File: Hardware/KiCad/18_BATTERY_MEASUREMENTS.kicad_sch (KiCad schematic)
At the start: 0 parts

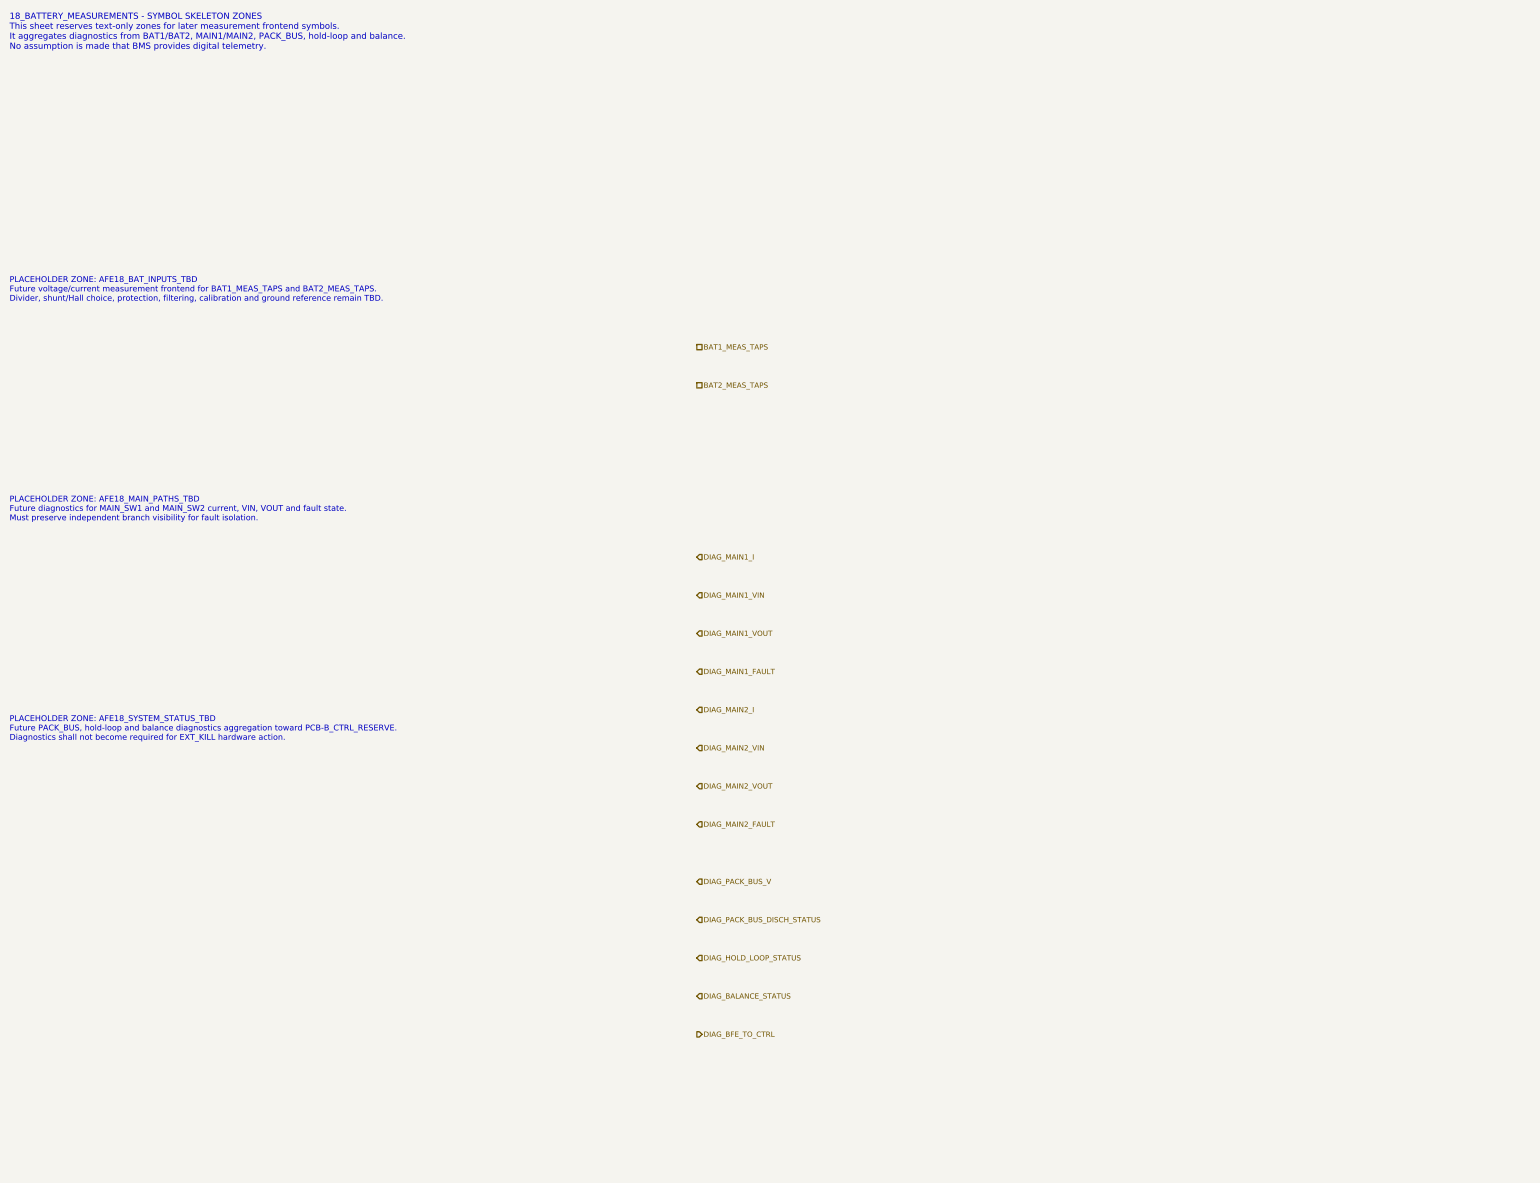
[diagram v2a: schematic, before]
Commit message: hardware: complete BFE measurement aggregation interfaces
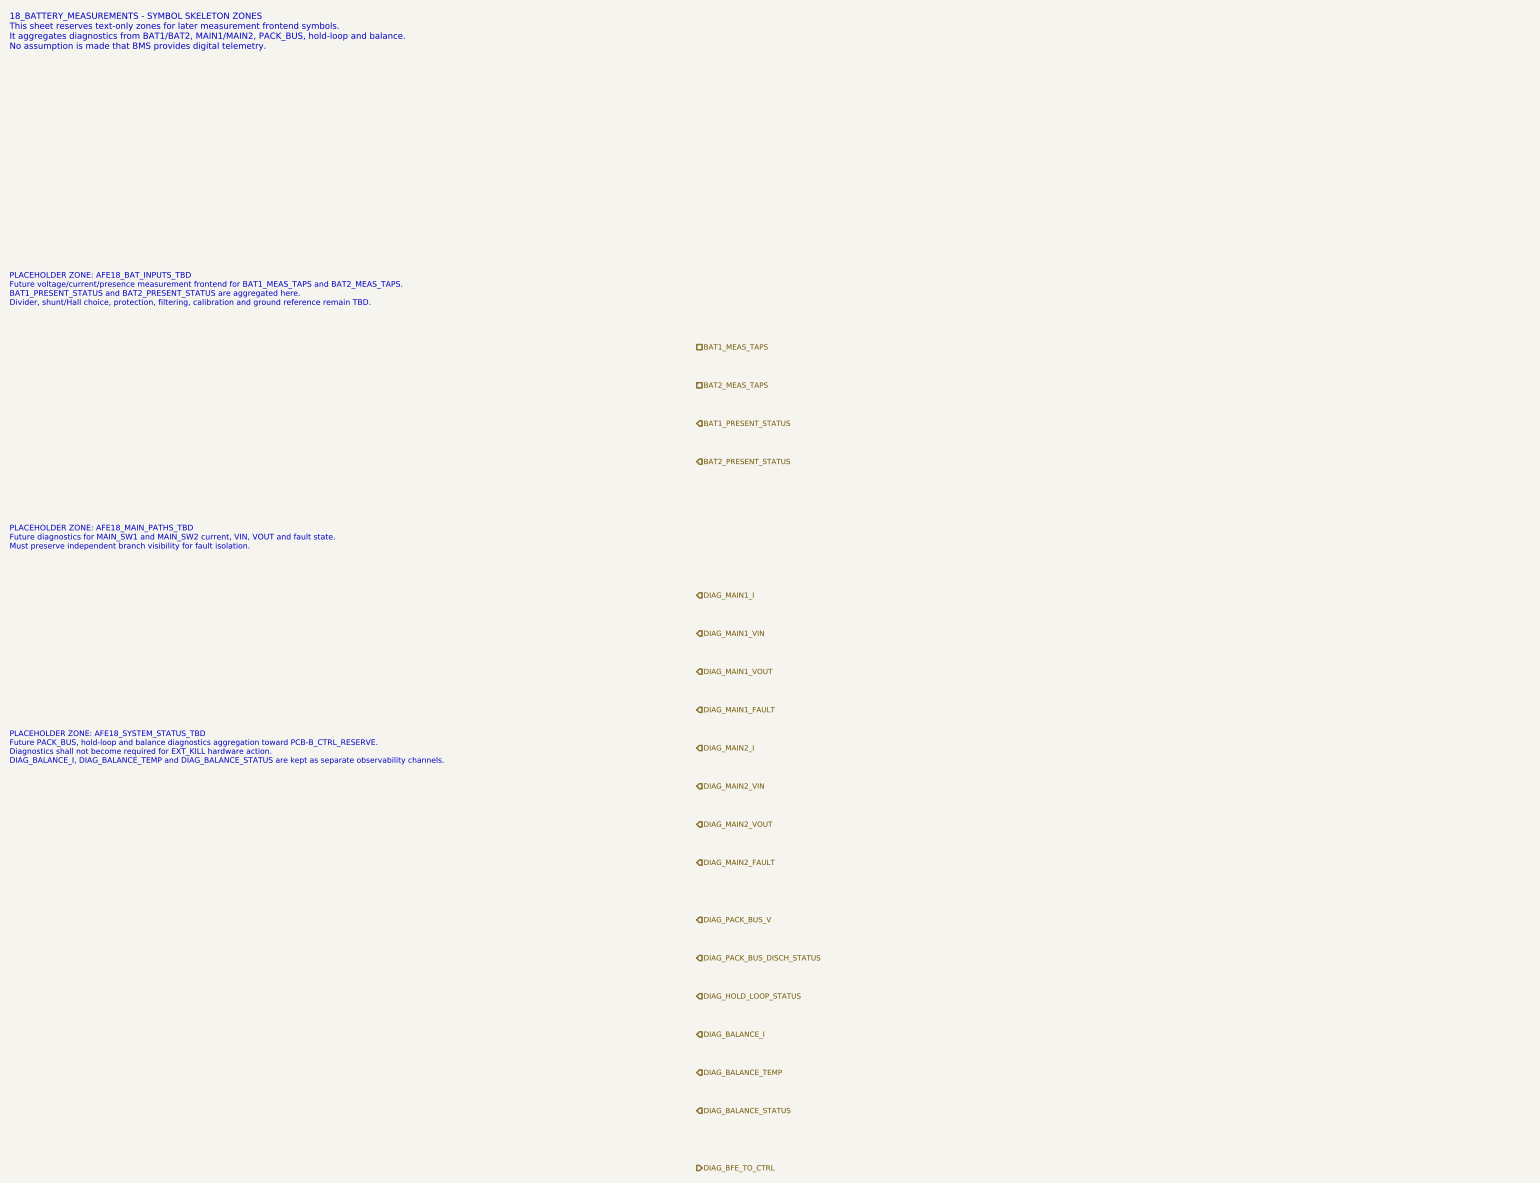
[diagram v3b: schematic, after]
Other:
- note added: "PLACEHOLDER ZONE: AFE18_BAT_INPUTS_TBD Future voltage/current/presence measurement frontend for BAT1_MEAS_TAPS and BAT2_MEAS_TAPS. BAT1_PRESENT_STATUS and BAT2_PRESENT_STATUS are aggregated here. Divider, shunt/Hall choice, protection, filtering, calibration and ground reference remain TBD."
- note added: "PLACEHOLDER ZONE: AFE18_SYSTEM_STATUS_TBD Future PACK_BUS, hold-loop and balance diagnostics aggregation toward PCB-B_CTRL_RESERVE. Diagnostics shall not become required for EXT_KILL hardware action. DIAG_BALANCE_I, DIAG_BALANCE_TEMP and DIAG_BALANCE_STATUS are kept as separate observability channels."
- note removed: "PLACEHOLDER ZONE: AFE18_BAT_INPUTS_TBD Future voltage/current measurement frontend for BAT1_MEAS_TAPS and BAT2_MEAS_TAPS. Divider, shunt/Hall choice, protection, filtering, calibration and ground reference remain TBD."
- note removed: "PLACEHOLDER ZONE: AFE18_SYSTEM_STATUS_TBD Future PACK_BUS, hold-loop and balance diagnostics aggregation toward PCB-B_CTRL_RESERVE. Diagnostics shall not become required for EXT_KILL hardware action."
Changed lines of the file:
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@@
 		(title "18_BATTERY_MEASUREMENTS - BFE sensing boundary")
 		(date "2026-07-15")
-		(rev "C1")
+		(rev "C2")
 		(company "Gonoboben/plataVM")
-		(comment 1 "Symbol skeleton: BFE measurement AFE and diagnostic placeholders")
+		(comment 1 "Interface consistency: complete BFE measurement aggregation")
 		(comment 2 "No ADC frontend, isolation, sensor technology or part number selected")
 	)
@@
 		(uuid "bfe-lb-00000018-0000-4000-8000-000000000101")
 	)
-	(text "PLACEHOLDER ZONE: AFE18_BAT_INPUTS_TBD\nFuture voltage/current measurement frontend for BAT1_MEAS_TAPS and BAT2_MEAS_TAPS.\nDivider, shunt/Hall choice, protection, filtering, calibration and ground reference remain TBD."
+	(text "PLACEHOLDER ZONE: AFE18_BAT_INPUTS_TBD\nFuture voltage/current/presence measurement frontend for BAT1_MEAS_TAPS and BAT2_MEAS_TAPS.\nBAT1_PRESENT_STATUS and BAT2_PRESENT_STATUS are aggregated here.\nDivider, shunt/Hall choice, protection, filtering, calibration and ground reference remain TBD."
 		(exclude_from_sim no)
 		(at 12 70 0)
-		(effects (font (size 1.22 1.22)) (justify left))
+		(effects (font (size 1.18 1.18)) (justify left))
 		(uuid "bfe-lb-00000018-0000-4000-8000-000000000102")
 	)
 	(text "PLACEHOLDER ZONE: AFE18_MAIN_PATHS_TBD\nFuture diagnostics for MAIN_SW1 and MAIN_SW2 current, VIN, VOUT and fault state.\nMust preserve independent branch visibility for fault isolation."
 		(exclude_from_sim no)
-		(at 12 116 0)
-		(effects (font (size 1.22 1.22)) (justify left))
+		(at 12 122 0)
+		(effects (font (size 1.18 1.18)) (justify left))
 		(uuid "bfe-lb-00000018-0000-4000-8000-000000000103")
 	)
-	(text "PLACEHOLDER ZONE: AFE18_SYSTEM_STATUS_TBD\nFuture PACK_BUS, hold-loop and balance diagnostics aggregation toward PCB-B_CTRL_RESERVE.\nDiagnostics shall not become required for EXT_KILL hardware action."
+	(text "PLACEHOLDER ZONE: AFE18_SYSTEM_STATUS_TBD\nFuture PACK_BUS, hold-loop and balance diagnostics aggregation toward PCB-B_CTRL_RESERVE.\nDiagnostics shall not become required for EXT_KILL hardware action.\nDIAG_BALANCE_I, DIAG_BALANCE_TEMP and DIAG_BALANCE_STATUS are kept as separate observability channels."
 		(exclude_from_sim no)
-		(at 12 162 0)
-		(effects (font (size 1.22 1.22)) (justify left))
+		(at 12 166 0)
+		(effects (font (size 1.16 1.16)) (justify left))
 		(uuid "bfe-lb-00000018-0000-4000-8000-000000000104")
 	)
 	(hierarchical_label "BAT1_MEAS_TAPS" (shape passive) (exclude_from_sim no) (at 156 82 0) (effects (font (size 1.1 1.1)) (justify left)) (uuid "bfe-lb-00000018-0000-4000-8000-000000000201"))
 	(hierarchical_label "BAT2_MEAS_TAPS" (shape passive) (exclude_from_sim no) (at 156 90 0) (effects (font (size 1.1 1.1)) (justify left)) (uuid "bfe-lb-00000018-0000-4000-8000-000000000202"))
-	(hierarchical_label "DIAG_MAIN1_I" (shape input) (exclude_from_sim no) (at 156 126 0) (effects (font (size 1.1 1.1)) (justify left)) (uuid "bfe-lb-00000018-0000-4000-8000-000000000203"))
-	(hierarchical_label "DIAG_MAIN1_VIN" (shape input) (exclude_from_sim no) (at 156 134 0) (effects (font (size 1.1 1.1)) (justify left)) (uuid "bfe-lb-00000018-0000-4000-8000-000000000204"))
-	(hierarchical_label "DIAG_MAIN1_VOUT" (shape input) (exclude_from_sim no) (at 156 142 0) (effects (font (size 1.1 1.1)) (justify left)) (uuid "bfe-lb-00000018-0000-4000-8000-000000000205"))
-	(hierarchical_label "DIAG_MAIN1_FAULT" (shape input) (exclude_from_sim no) (at 156 150 0) (effects (font (size 1.1 1.1)) (justify left)) (uuid "bfe-lb-00000018-0000-4000-8000-000000000206"))
-	(hierarchical_label "DIAG_MAIN2_I" (shape input) (exclude_from_sim no) (at 156 158 0) (effects (font (size 1.1 1.1)) (justify left)) (uuid "bfe-lb-00000018-0000-4000-8000-000000000207"))
-	(hierarchical_label "DIAG_MAIN2_VIN" (shape input) (exclude_from_sim no) (at 156 166 0) (effects (font (size 1.1 1.1)) (justify left)) (uuid "bfe-lb-00000018-0000-4000-8000-000000000208"))
-	(hierarchical_label "DIAG_MAIN2_VOUT" (shape input) (exclude_from_sim no) (at 156 174 0) (effects (font (size 1.1 1.1)) (justify left)) (uuid "bfe-lb-00000018-0000-4000-8000-000000000209"))
-	(hierarchical_label "DIAG_MAIN2_FAULT" (shape input) (exclude_from_sim no) (at 156 182 0) (effects (font (size 1.1 1.1)) (justify left)) (uuid "bfe-lb-00000018-0000-4000-8000-000000000210"))
-	(hierarchical_label "DIAG_PACK_BUS_V" (shape input) (exclude_from_sim no) (at 156 194 0) (effects (font (size 1.1 1.1)) (justify left)) (uuid "bfe-lb-00000018-0000-4000-8000-000000000211"))
-	(hierarchical_label "DIAG_PACK_BUS_DISCH_STATUS" (shape input) (exclude_from_sim no) (at 156 202 0) (effects (font (size 1.1 1.1)) (justify left)) (uuid "bfe-lb-00000018-0000-4000-8000-000000000212"))
-	(hierarchical_label "DIAG_HOLD_LOOP_STATUS" (shape input) (exclude_from_sim no) (at 156 210 0) (effects (font (size 1.1 1.1)) (justify left)) (uuid "bfe-lb-00000018-0000-4000-8000-000000000213"))
-	(hierarchical_label "DIAG_BALANCE_STATUS" (shape input) (exclude_from_sim no) (at 156 218 0) (effects (font (size 1.1 1.1)) (justify left)) (uuid "bfe-lb-00000018-0000-4000-8000-000000000214"))
-	(hierarchical_label "DIAG_BFE_TO_CTRL" (shape output) (exclude_from_sim no) (at 156 226 0) (effects (font (size 1.1 1.1)) (justify left)) (uuid "bfe-lb-00000018-0000-4000-8000-000000000215"))
+	(hierarchical_label "BAT1_PRESENT_STATUS" (shape input) (exclude_from_sim no) (at 156 98 0) (effects (font (size 1.1 1.1)) (justify left)) (uuid "bfe-lb-00000018-0000-4000-8000-000000000216"))
+	(hierarchical_label "BAT2_PRESENT_STATUS" (shape input) (exclude_from_sim no) (at 156 106 0) (effects (font (size 1.1 1.1)) (justify left)) (uuid "bfe-lb-00000018-0000-4000-8000-000000000217"))
+	(hierarchical_label "DIAG_MAIN1_I" (shape input) (exclude_from_sim no) (at 156 134 0) (effects (font (size 1.1 1.1)) (justify left)) (uuid "bfe-lb-00000018-0000-4000-8000-000000000203"))
+	(hierarchical_label "DIAG_MAIN1_VIN" (shape input) (exclude_from_sim no) (at 156 142 0) (effects (font (size 1.1 1.1)) (justify left)) (uuid "bfe-lb-00000018-0000-4000-8000-000000000204"))
+	(hierarchical_label "DIAG_MAIN1_VOUT" (shape input) (exclude_from_sim no) (at 156 150 0) (effects (font (size 1.1 1.1)) (justify left)) (uuid "bfe-lb-00000018-0000-4000-8000-000000000205"))
+	(hierarchical_label "DIAG_MAIN1_FAULT" (shape input) (exclude_from_sim no) (at 156 158 0) (effects (font (size 1.1 1.1)) (justify left)) (uuid "bfe-lb-00000018-0000-4000-8000-000000000206"))
+	(hierarchical_label "DIAG_MAIN2_I" (shape input) (exclude_from_sim no) (at 156 166 0) (effects (font (size 1.1 1.1)) (justify left)) (uuid "bfe-lb-00000018-0000-4000-8000-000000000207"))
+	(hierarchical_label "DIAG_MAIN2_VIN" (shape input) (exclude_from_sim no) (at 156 174 0) (effects (font (size 1.1 1.1)) (justify left)) (uuid "bfe-lb-00000018-0000-4000-8000-000000000208"))
+	(hierarchical_label "DIAG_MAIN2_VOUT" (shape input) (exclude_from_sim no) (at 156 182 0) (effects (font (size 1.1 1.1)) (justify left)) (uuid "bfe-lb-00000018-0000-4000-8000-000000000209"))
+	(hierarchical_label "DIAG_MAIN2_FAULT" (shape input) (exclude_from_sim no) (at 156 190 0) (effects (font (size 1.1 1.1)) (justify left)) (uuid "bfe-lb-00000018-0000-4000-8000-000000000210"))
+	(hierarchical_label "DIAG_PACK_BUS_V" (shape input) (exclude_from_sim no) (at 156 202 0) (effects (font (size 1.1 1.1)) (justify left)) (uuid "bfe-lb-00000018-0000-4000-8000-000000000211"))
+	(hierarchical_label "DIAG_PACK_BUS_DISCH_STATUS" (shape input) (exclude_from_sim no) (at 156 210 0) (effects (font (size 1.1 1.1)) (justify left)) (uuid "bfe-lb-00000018-0000-4000-8000-000000000212"))
+	(hierarchical_label "DIAG_HOLD_LOOP_STATUS" (shape input) (exclude_from_sim no) (at 156 218 0) (effects (font (size 1.1 1.1)) (justify left)) (uuid "bfe-lb-00000018-0000-4000-8000-000000000213"))
+	(hierarchical_label "DIAG_BALANCE_I" (shape input) (exclude_from_sim no) (at 156 226 0) (effects (font (size 1.1 1.1)) (justify left)) (uuid "bfe-lb-00000018-0000-4000-8000-000000000218"))
+	(hierarchical_label "DIAG_BALANCE_TEMP" (shape input) (exclude_from_sim no) (at 156 234 0) (effects (font (size 1.1 1.1)) (justify left)) (uuid "bfe-lb-00000018-0000-4000-8000-000000000219"))
+	(hierarchical_label "DIAG_BALANCE_STATUS" (shape input) (exclude_from_sim no) (at 156 242 0) (effects (font (size 1.1 1.1)) (justify left)) (uuid "bfe-lb-00000018-0000-4000-8000-000000000214"))
+	(hierarchical_label "DIAG_BFE_TO_CTRL" (shape output) (exclude_from_sim no) (at 156 254 0) (effects (font (size 1.1 1.1)) (justify left)) (uuid "bfe-lb-00000018-0000-4000-8000-000000000215"))
 )
